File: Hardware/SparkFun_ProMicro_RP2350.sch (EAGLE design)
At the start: 61 parts, among them J2 QWIIC_RIGHT_ANGLE, J5 USB Female Type C Connector, U1 RT9080-33GJ5, U2 RP2350A, U3 WS2812-2020, U4 W25QXX128MBIT, Y1 12MHz

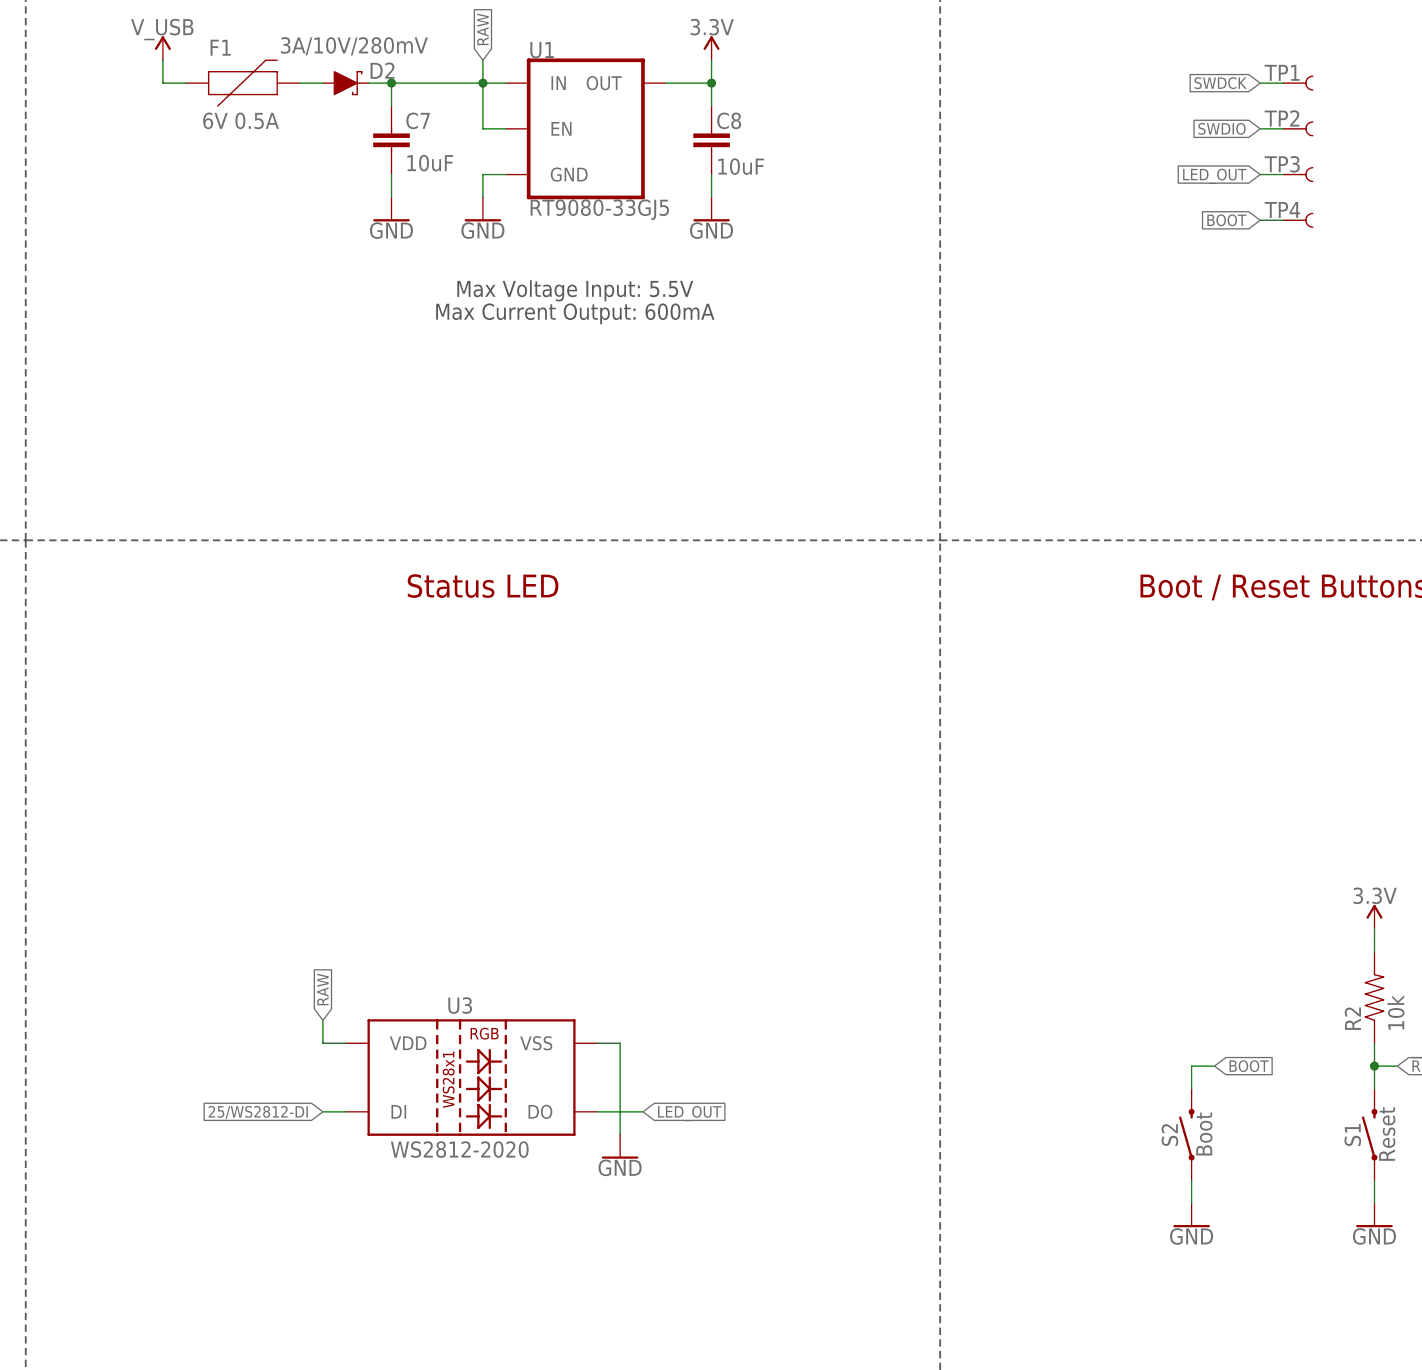
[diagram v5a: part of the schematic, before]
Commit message: Update WS2812 symbol
Use new version so Eagle stops complaining
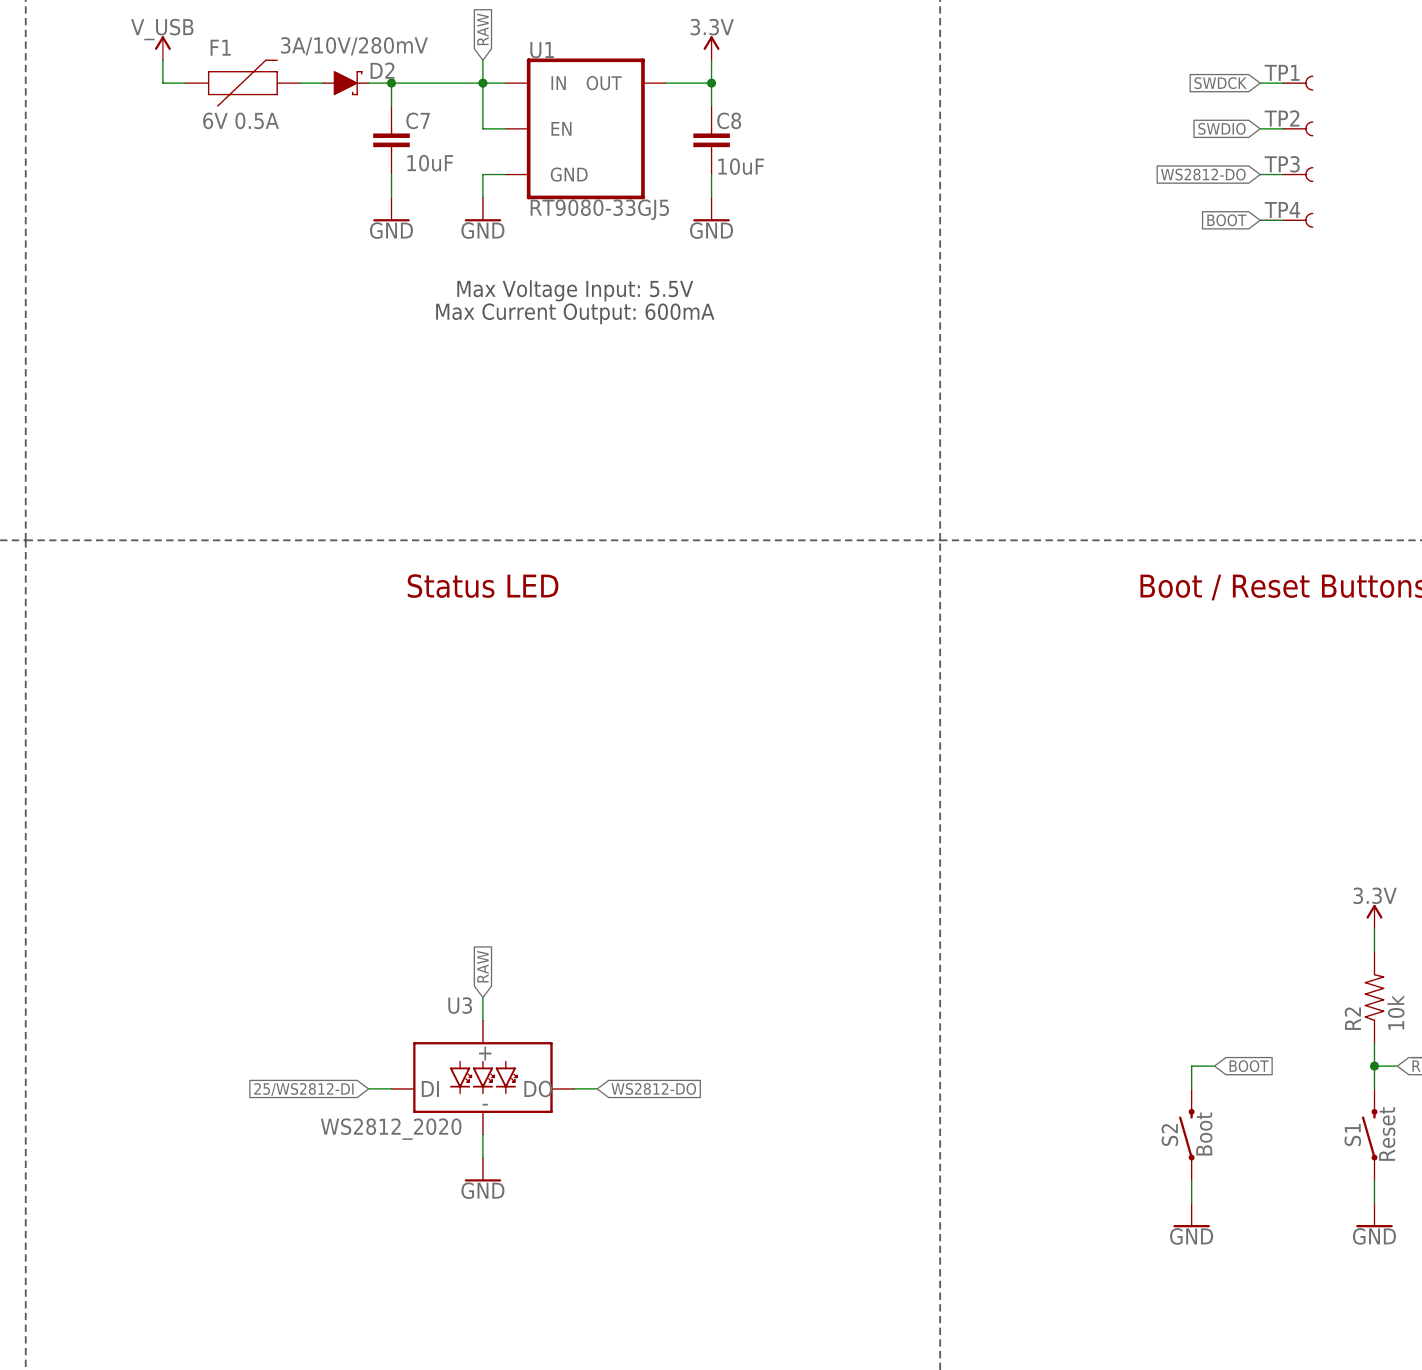
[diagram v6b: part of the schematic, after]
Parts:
- U3: value WS2812-2020 -> WS2812_2020; device SparkFun-LED:WS2812-2020 -> SparkFun-LED:WS2812_2020
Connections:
- net LED_OUT renamed WS2812-DO
- net GND: now also U3.GND; no longer U3.VSS
- net RAW: now also U3.VCC; no longer U3.VDD
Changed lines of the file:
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@@
 <part name="TP1" library="SparkFun-Connectors" deviceset="TEST-POINT" device="3X5" value="TEST-POINT3X5"/>
 <part name="TP2" library="SparkFun-Connectors" deviceset="TEST-POINT" device="3X5" value="TEST-POINT3X5"/>
-<part name="U3" library="SparkFun-LED" deviceset="WS2812-2020" device=""/>
+<part name="U3" library="SparkFun-LED" deviceset="WS2812" device="_2020"/>
 <part name="GND4" library="SparkFun-PowerSymbols" deviceset="GND" device=""/>
 <part name="FRAME2" library="SparkFun-Aesthetics" deviceset="FRAME-LEDGER" device="">
@@
 <instance part="U3" gate="G$1" x="203.2" y="129.54" smashed="yes">
 <attribute name="NAME" x="200.66" y="137.922" size="1.778" layer="95" font="vector" align="bottom-center"/>
-<attribute name="VALUE" x="200.66" y="121.92" size="1.778" layer="95" font="vector" align="bottom-center"/>
-</instance>
-<instance part="GND4" gate="1" x="218.44" y="121.92" smashed="yes">
-<attribute name="VALUE" x="218.44" y="121.666" size="1.778" layer="96" align="top-center"/>
+<attribute name="VALUE" x="193.04" y="124.46" size="1.778" layer="95" font="vector" align="bottom-center"/>
+</instance>
+<instance part="GND4" gate="1" x="203.2" y="119.38" smashed="yes">
+<attribute name="VALUE" x="203.2" y="119.126" size="1.778" layer="96" align="top-center"/>
 </instance>
 <instance part="FRAME2" gate="G$1" x="0" y="0" smashed="yes"/>
@@
 </segment>
 <segment>
-<pinref part="U3" gate="G$1" pin="VSS"/>
-<wire x1="215.9" y1="134.62" x2="218.44" y2="134.62" width="0.1524" layer="91"/>
-<wire x1="218.44" y1="134.62" x2="218.44" y2="124.46" width="0.1524" layer="91"/>
+<wire x1="203.2" y1="124.46" x2="203.2" y2="121.92" width="0.1524" layer="91"/>
 <pinref part="GND4" gate="1" pin="GND"/>
+<pinref part="U3" gate="G$1" pin="GND"/>
 </segment>
 <segment>
@@
 </segment>
 <segment>
-<pinref part="U3" gate="G$1" pin="VDD"/>
-<wire x1="187.96" y1="134.62" x2="185.42" y2="134.62" width="0.1524" layer="91"/>
-<wire x1="185.42" y1="134.62" x2="185.42" y2="137.16" width="0.1524" layer="91"/>
-<label x="185.42" y="137.16" size="1.27" layer="95" rot="R90" xref="yes"/>
+<wire x1="203.2" y1="137.16" x2="203.2" y2="139.7" width="0.1524" layer="91"/>
+<label x="203.2" y="139.7" size="1.27" layer="95" rot="R90" xref="yes"/>
+<pinref part="U3" gate="G$1" pin="VCC"/>
 </segment>
 </net>
@@
 </segment>
 <segment>
+<wire x1="193.04" y1="129.54" x2="190.5" y2="129.54" width="0.1524" layer="91"/>
+<label x="190.5" y="129.54" size="1.27" layer="95" rot="R180" xref="yes"/>
 <pinref part="U3" gate="G$1" pin="DI"/>
-<wire x1="187.96" y1="127" x2="185.42" y2="127" width="0.1524" layer="91"/>
-<label x="185.42" y="127" size="1.27" layer="95" rot="R180" xref="yes"/>
-</segment>
-</net>
-<net name="LED_OUT" class="0">
+</segment>
+</net>
+<net name="WS2812-DO" class="0">
 <segment>
 <pinref part="TP3" gate="G$1" pin="1"/>
@@
 </segment>
 <segment>
-<label x="220.98" y="127" size="1.27" layer="95" font="vector" xref="yes"/>
+<label x="215.9" y="129.54" size="1.27" layer="95" font="vector" xref="yes"/>
+<wire x1="215.9" y1="129.54" x2="213.36" y2="129.54" width="0.1524" layer="91"/>
 <pinref part="U3" gate="G$1" pin="DO"/>
-<wire x1="220.98" y1="127" x2="215.9" y2="127" width="0.1524" layer="91"/>
-</segment>
-</net>
+</segment>
+</net>

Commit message: Use castellated pad device from SparkFun lib
Remove dependency of "Castellated" lib
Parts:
- J3, J4: device Castellated:CONN_12CASTLE -> SparkFun-Connectors:CONN_12CASTELLATED
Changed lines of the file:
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@@
 <part name="SUPPLY9" library="SparkFun-PowerSymbols" deviceset="V_USB" device=""/>
 <part name="GND16" library="SparkFun-PowerSymbols" deviceset="GND" device=""/>
-<part name="J3" library="Castellated" deviceset="CONN_12" device="CASTLE"/>
-<part name="J4" library="Castellated" deviceset="CONN_12" device="CASTLE"/>
+<part name="J3" library="SparkFun-Connectors" deviceset="CONN_12" device="CASTELLATED"/>
+<part name="J4" library="SparkFun-Connectors" deviceset="CONN_12" device="CASTELLATED"/>
 <part name="LOGO3" library="SparkFun-Aesthetics" deviceset="QWIIC_LOGO" device="_6MM" value="QWIIC_LOGO_6MM"/>
 <part name="R5" library="SparkFun-Resistors" deviceset="2.2KOHM" device="-0402T-1/16W-1%" value="2.2k"/>
